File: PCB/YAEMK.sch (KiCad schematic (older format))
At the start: 222 parts, among them J1 DBG, P1 PC, P2 Link, P3 SSD1107, Q1 MMUN2133LT1G, Q2 DMMT5401, Q3 AO3401A, SW1 ALPS EC11, U1 24LC64, U2 SSP6206, U3 USBLC6-2SC6, U4 USBLC6-2SC6, U5 STM32F303CCTx

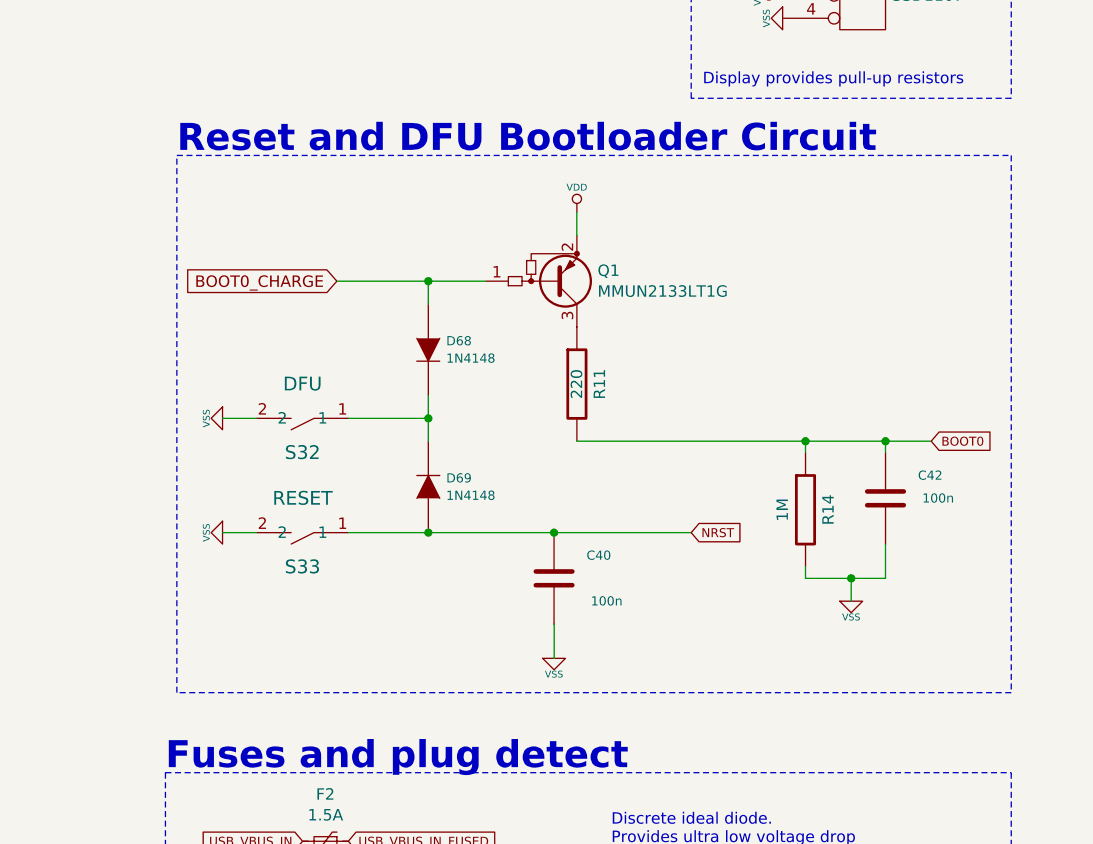
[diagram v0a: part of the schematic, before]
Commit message: Update Reset / DFU circut to single button version
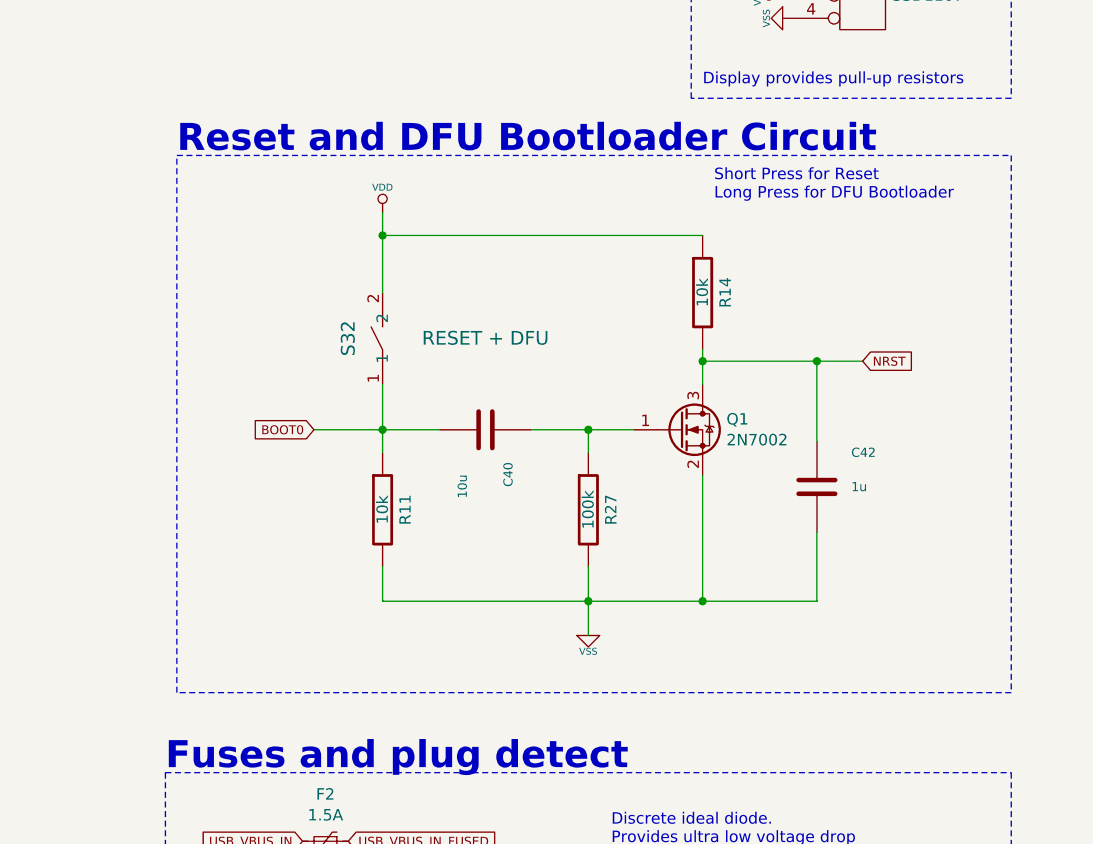
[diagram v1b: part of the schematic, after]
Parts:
- removed D68, D69: 1N4148, prettylib:D_SOD-523, symbol YAEMK:DIODE
- removed Q1: MMUN2133LT1G, prettylib:SOT-23, symbol Device:Q_PNP_BEC_BRT
- removed S33: RESET, prettylib:SMD_Tacticle_Switch_TS24CA_flipable, symbol YAEMK:SW
- added Q1: 2N7002, prettylib:SOT-23, symbol YAEMK:2N7002
- added R27: 100k, prettylib:SMD-0603, symbol YAEMK:R
- C40: value 100n -> 10u; LCSC Part C14663 -> C19702
- C42: value 100n -> 1u; LCSC Part C14663 -> C15849
- G1, G2, MH10, MH11, MH12: JLCPCB BOM (none) -> 0
- R11: value 220 -> 10k; LCSC Part C22962 -> C25804
- R14: value 1M -> 10k; LCSC Part C22935 -> C25804
- S32: value DFU -> RESET + DFU
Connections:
- net BOOT0: now also C40.1, R11.1, S32.1; no longer C42.2, R11.2, R14.1
- net NRST: now also C42.1, R14.2, Q1.3 (D); no longer C40.2
- net VDD: now also R14.1, S32.2
- net VSS: now also C42.2, R11.2, Q1.2 (S), R27.2; no longer C40.1, C42.1, R14.2, S32.2
- new net: C40.2, Q1.1 (G), R27.1
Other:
- note added: "Short Press for Reset\nLong Press for DFU Bootloader"
- moved on the sheet: C40, R11

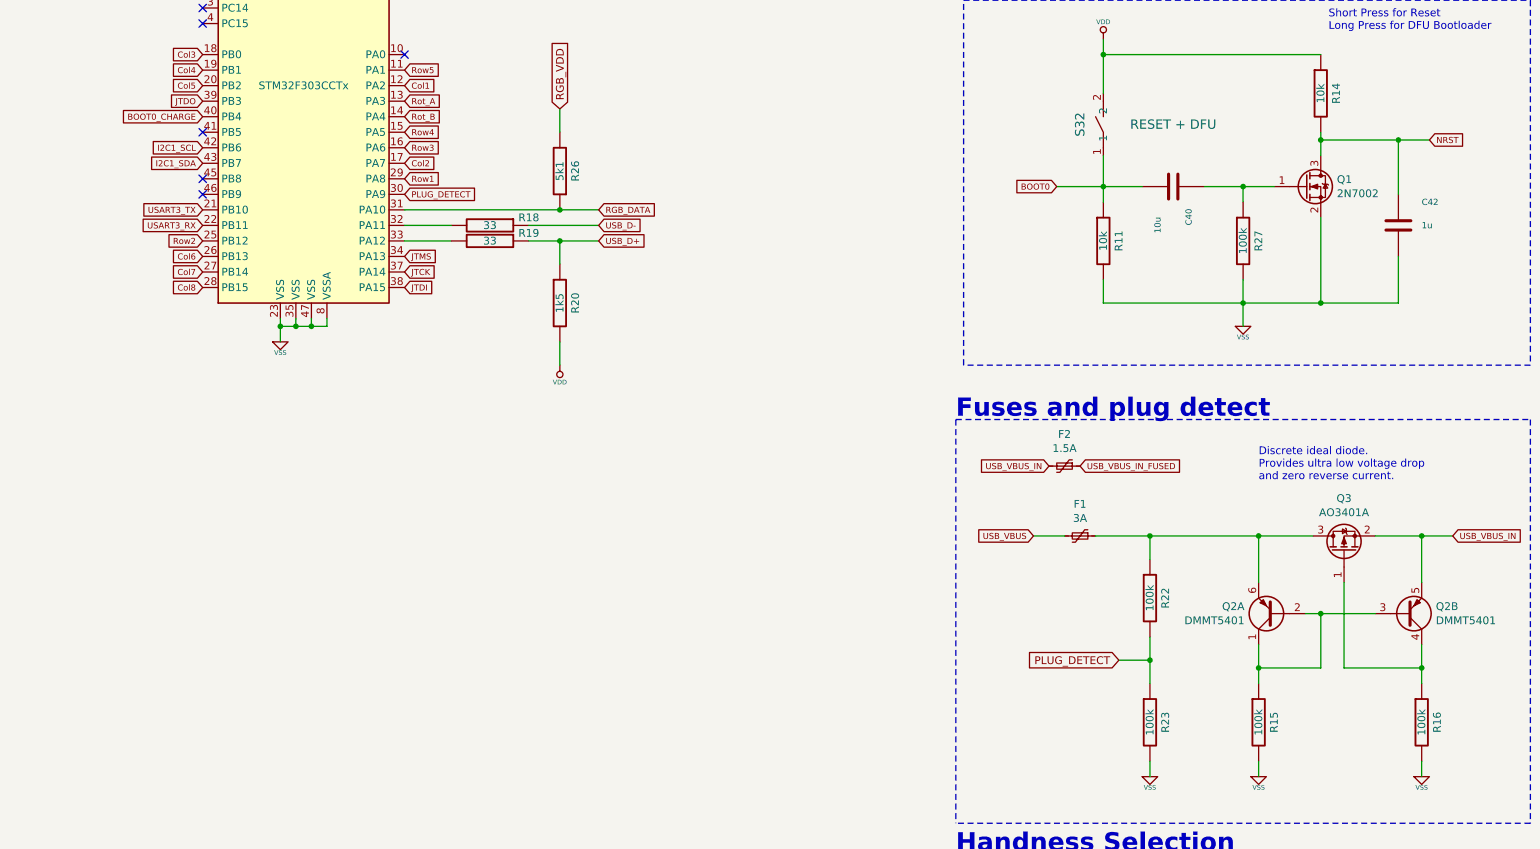
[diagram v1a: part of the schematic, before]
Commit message: Update Plugdetect Values
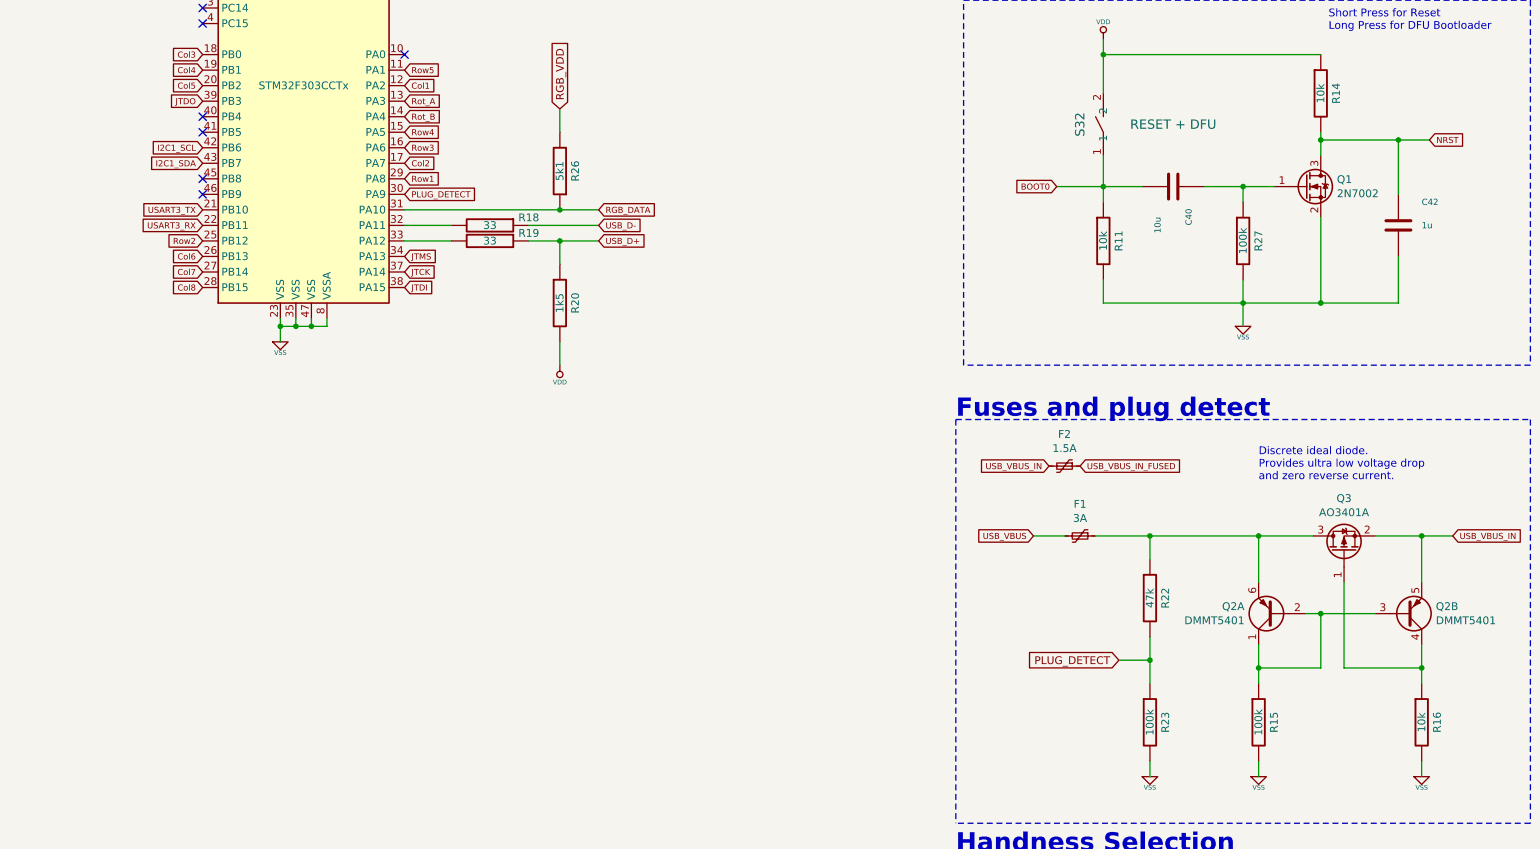
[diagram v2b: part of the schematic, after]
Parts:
- Q3: LCSC Part C15127 -> C142520
- R16: value 100k -> 10k
- R22: value 100k -> 47k
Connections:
- net BOOT0_CHARGE: no longer names the net of U5.40 (PB4)
- no-connect marks 14 -> 15
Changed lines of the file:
@@
 Text GLabel 15650 7300 2    39   Input ~ 0
 JTDI
-Text GLabel 14350 6200 0    39   Input ~ 0
-BOOT0_CHARGE
 Wire Notes Line
 	9400 800  9400 2900
@@
 P 22200 10100
 F 0 "R16" V 22300 10100 50  0000 C CNN
-F 1 "100k" V 22200 10100 50  0000 C CNN
+F 1 "10k" V 22200 10100 50  0000 C CNN
 F 2 "prettylib:SMD-0603" V 22100 10100 60  0001 C CNN
 F 3 "" H 22200 10100 60  0001 C CNN
@@
 F 2 "prettylib:SOT-23" H 21900 8925 50  0001 L CIN
 F 3 "http://www.aosmd.com/pdfs/datasheet/AO3401A.pdf" H 21700 9000 50  0001 L CNN
-F 4 " C15127 " H 21700 9000 50  0001 C CNN "LCSC Part"
+F 4 " C142520" H 21700 9000 50  0001 C CNN "LCSC Part"
 F 5 "1" H 21700 9000 50  0001 C CNN "JLCPCB BOM"
 	1    21700 9000
@@
 P 20450 9300
 F 0 "R22" V 20550 9300 50  0000 C CNN
-F 1 "100k" V 20450 9300 50  0000 C CNN
+F 1 "47k" V 20450 9300 50  0000 C CNN
 F 2 "prettylib:SMD-0603" V 20350 9300 60  0001 C CNN
 F 3 "" H 20450 9300 60  0001 C CNN
@@
 Text Notes 21600 5650 0    50   ~ 0
 Short Press for Reset\nLong Press for DFU Bootloader
+NoConn ~ 14350 6200
 $EndSCHEMATC

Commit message: Add opamp ideal diode
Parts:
- removed Q2: DMMT5401, prettylib:SOT-23-6, symbol Device:Q_DUAL_PNP_PNP_C1B1B2C2E2E1
- removed R15: 100k, prettylib:SMD-0603, symbol YAEMK:R
- removed R16: 10k, prettylib:SMD-0603, symbol YAEMK:R
- removed U3, U4: USBLC6-2SC6, prettylib:SOT-23-6, symbol YAEMK:USBLC6-2SC6
- added U3, U4: USBLC6-4SC6, prettylib:SOT-23-6, symbol Power_Protection:USBLC6-4SC6
- added U6: LMV321, prettylib:SOT-23-5, symbol Amplifier_Operational:LMV321
- C45: value 100n -> 10u; footprint prettylib:SMD-0603 -> prettylib:SMD-0805; LCSC Part C14663 -> C15850
- D1, D10, D11, D12, D13, D14, D15, D16, D17, D18, D19, D2, D20, D21, D22, D23, D24, D25, D26, D27, D28, D29, D3, D30, D31, D32, D33, D34, D4, D5, D6, D7, D8, D9: footprint prettylib:D_SOD-523 -> Diode_SMD:D_SOD-123
- R22: value 47k -> 100k
- R23: value 100k -> 200k; LCSC Part C25803 -> C25811
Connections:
- net ESD_LINK+ is gone; now on net LINK+: P2.A6 (D+), P2.B6 (D+)
- net ESD_LINK- is gone; now on net LINK-: P2.A7 (D-), P2.B7 (D-)
- net ESD_USB_D+ is gone; now on net USB_D+: P1.A6 (D+), P1.B6 (D+)
- net ESD_USB_D- is gone; now on net USB_D-: P1.A7 (D-), P1.B7 (D-)
- net LINK+: now also U4.3 (I/O2)
- net LINK-: now also U4.1 (I/O1)
- net RGB_VDD: now also U6.1 (+), U6.5 (V+)
- net USB_D+: now also U3.3 (I/O2)
- net USB_D-: now also U3.1 (I/O1)
- net USB_VBUS: now also U3.5 (VBUS)
- net USB_VBUS_IN_FUSED: now also U4.5 (VBUS)
- net VSS: now also U3.2 (GND), U4.2 (GND), U6.2 (V-)
- net at F1.1, Q3.3 (D), R22.1: now also U6.3 (-)
- net at Q3.1 (G): now also U6.4
- no-connect marks 15 -> 19
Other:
- moved on the sheet: Q3

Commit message: RC for real
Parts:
- C43, C44, C45: footprint prettylib:SMD-0805 -> prettylib:SMD-0603
- C46, C47: value 12p -> 20p; LCSC Part C38523 -> C1648
- D1, D10, D11, D12, D13, D14, D15, D16, D17, D18, D19, D2, D20, D21, D22, D23, D24, D25, D26, D27, D28, D29, D3, D30, D31, D32, D33, D34, D4, D5, D6, D7, D8, D9: footprint Diode_SMD:D_SOD-123 -> prettylib:D_SOD-123; LCSC Part C68948 -> C81598
- F1: LCSC Part C118413 -> C70085
- F2: LCSC Part C99563 -> C70081
- HSE1: LCSC Part C648984 -> C403948
- Q3: LCSC Part C142520 -> C15127
- R18, R19: LCSC Part C23138 -> C23140
- U1: value 24LC64 -> CAT24C512; LCSC Part C189763 -> C56096
- U3, U4: value USBLC6-4SC6 -> SRV0504; JLCPCB BOM (none) -> 1; LCSC Part (none) -> C384888

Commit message: Update ESD Diode, clean libs
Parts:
- C40: LCSC Part C19702 -> C19702
- C43, C44, C45: LCSC Part C15850 -> C19702
- U2: value SSP6206 -> XC6206P332MR
- U3, U4: symbol Power_Protection:USBLC6-4SC6 -> YAEMK:SRV0504
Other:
- note added: "MCU STM32F303 or STM32F103"
- note removed: "MCU F103, F303 or GDVF103"
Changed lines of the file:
@@
 F 2 "prettylib:SMD-0603" H 8288 4950 30  0001 C CNN
 F 3 "" H 8250 5100 60  0000 C CNN
-F 4 "C15850" H 8250 5100 50  0001 C CNN "LCSC Part"
+F 4 "C19702" H 8250 5100 50  0001 C CNN "LCSC Part"
 F 5 "1" H 8250 5100 50  0001 C CNN "JLCPCB BOM"
 	1    8250 5100
@@
 F 2 "prettylib:SMD-0603" H 9388 4950 30  0001 C CNN
 F 3 "" H 9350 5100 60  0000 C CNN
-F 4 "C15850" H 9350 5100 50  0001 C CNN "LCSC Part"
+F 4 "C19702" H 9350 5100 50  0001 C CNN "LCSC Part"
 F 5 "1" H 9350 5100 50  0001 C CNN "JLCPCB BOM"
 	1    9350 5100
@@
 USB_D+
 Wire Wire Line
-	14950 1050 14850 1050
+	14950 1050 14900 1050
 Wire Wire Line
 	15450 1050 15350 1050
@@
 F 2 "prettylib:SMD-0603" H 15188 900 30  0001 C CNN
 F 3 "" H 15150 1050 60  0000 C CNN
-F 4 "C15850" H 15150 1050 50  0001 C CNN "LCSC Part"
+F 4 "C19702" H 15150 1050 50  0001 C CNN "LCSC Part"
 F 5 "1" H 15150 1050 50  0001 C CNN "JLCPCB BOM"
 	1    15150 1050
@@
 Text GLabel 12850 1050 0    39   Input ~ 0
 USB_VBUS
-Text GLabel 14850 2200 3    39   Input ~ 0
+Text GLabel 14900 2200 3    39   Input ~ 0
 VSS
 Text Notes 12000 800  0    118  ~ 24
@@
 Text GLabel 14700 1050 0    39   Input ~ 0
 USB_VBUS_IN_FUSED
-Connection ~ 14850 1050
-Wire Wire Line
-	14850 1050 14700 1050
+Connection ~ 14900 1050
+Wire Wire Line
+	14900 1050 14700 1050
 Wire Wire Line
 	12950 1050 12850 1050
@@
 P 8800 4800
 F 0 "U2" H 8800 5042 50  0000 C CNN
-F 1 "SSP6206" H 8800 4951 50  0000 C CNN
+F 1 "XC6206P332MR" H 8800 4951 50  0000 C CNN
 F 2 "prettylib:SOT-23" H 8800 5000 50  0001 C CNN
 F 3 "" H 8900 4550 50  0001 C CNN
@@
 Wire Notes Line
 	12000 800  15800 800
-Text Notes 15550 14700 0    118  ~ 24
+Text Notes 15550 14750 0    118  ~ 24
 JLC PCBA Holes
-Text Notes 14200 14800 0    118  ~ 24
+Text Notes 14250 14850 0    118  ~ 24
 YAEMK Logos
 Wire Notes Line
@@
 Wire Wire Line
 	7550 11400 7550 11550
-Text Notes 13800 4000 0    118  ~ 24
-MCU F103, F303 or GDVF103
+Text Notes 13600 4000 0    118  ~ 24
+MCU STM32F303 or STM32F103
 Wire Notes Line
 	19200 12450 21500 12450
@@
 F 2 "prettylib:SMD-0603" H 20638 6500 30  0001 C CNN
 F 3 "" H 20600 6650 60  0000 C CNN
-F 4 " C19702" H 20600 6650 50  0001 C CNN "LCSC Part"
+F 4 "C19702" H 20600 6650 50  0001 C CNN "LCSC Part"
 F 5 "1" H 20600 6650 50  0001 C CNN "JLCPCB BOM"
 	1    20600 6650
@@
 $EndComp
 $Comp
-L Power_Protection:USBLC6-4SC6 U3
+L YAEMK:SRV0504 U3
 U 1 1 609C60B5
 P 12950 1700
 F 0 "U3" H 12950 2281 50  0000 C CNN
-F 1 "SRV0504" H 12950 2190 50  0000 C CNN
+F 1 "SRV0504" H 13200 1300 50  0000 C CNN
 F 2 "prettylib:SOT-23-6" H 12950 1200 50  0001 C CNN
 F 3 "" H 13150 2050 50  0001 C CNN
@@
 $EndComp
 Wire Wire Line
-	12950 1050 12950 1300
+	12950 1050 12950 1200
 Wire Wire Line
 	12950 2200 12950 2100
@@
 NoConn ~ 13350 1800
 $Comp
-L Power_Protection:USBLC6-4SC6 U4
+L YAEMK:SRV0504 U4
 U 1 1 60B72425
-P 14850 1700
-F 0 "U4" H 14850 2281 50  0000 C CNN
-F 1 "SRV0504" H 14850 2190 50  0000 C CNN
-F 2 "prettylib:SOT-23-6" H 14850 1200 50  0001 C CNN
-F 3 "" H 15050 2050 50  0001 C CNN
-F 4 "1" H 14850 1700 50  0001 C CNN "JLCPCB BOM"
-F 5 " C384888" H 14850 1700 50  0001 C CNN "LCSC Part"
-	1    14850 1700
-	1    0    0    -1
-$EndComp
-NoConn ~ 15250 1600
-NoConn ~ 15250 1800
-Wire Wire Line
-	14350 1600 14450 1600
-Wire Wire Line
-	14450 1800 14350 1800
-Wire Wire Line
-	14850 1050 14850 1300
-Wire Wire Line
-	14850 2200 14850 2100
+P 14900 1700
+F 0 "U4" H 14900 2281 50  0000 C CNN
+F 1 "SRV0504" H 15200 1300 50  0000 C CNN
+F 2 "prettylib:SOT-23-6" H 14900 1200 50  0001 C CNN
+F 3 "" H 15100 2050 50  0001 C CNN
+F 4 "1" H 14900 1700 50  0001 C CNN "JLCPCB BOM"
+F 5 " C384888" H 14900 1700 50  0001 C CNN "LCSC Part"
+	1    14900 1700
+	1    0    0    -1
+$EndComp
+NoConn ~ 15300 1600
+NoConn ~ 15300 1800
+Wire Wire Line
+	14350 1600 14500 1600
+Wire Wire Line
+	14500 1800 14350 1800
+Wire Wire Line
+	14900 1050 14900 1200
+Wire Wire Line
+	14900 2200 14900 2100
 $EndSCHEMATC

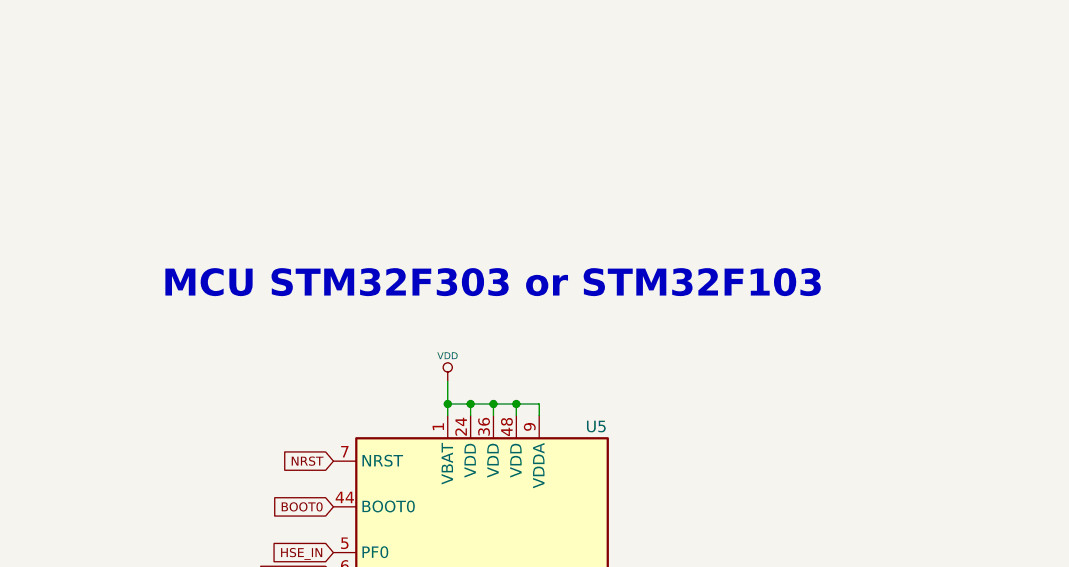
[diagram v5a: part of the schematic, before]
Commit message: Add GD32VF103 to schematic
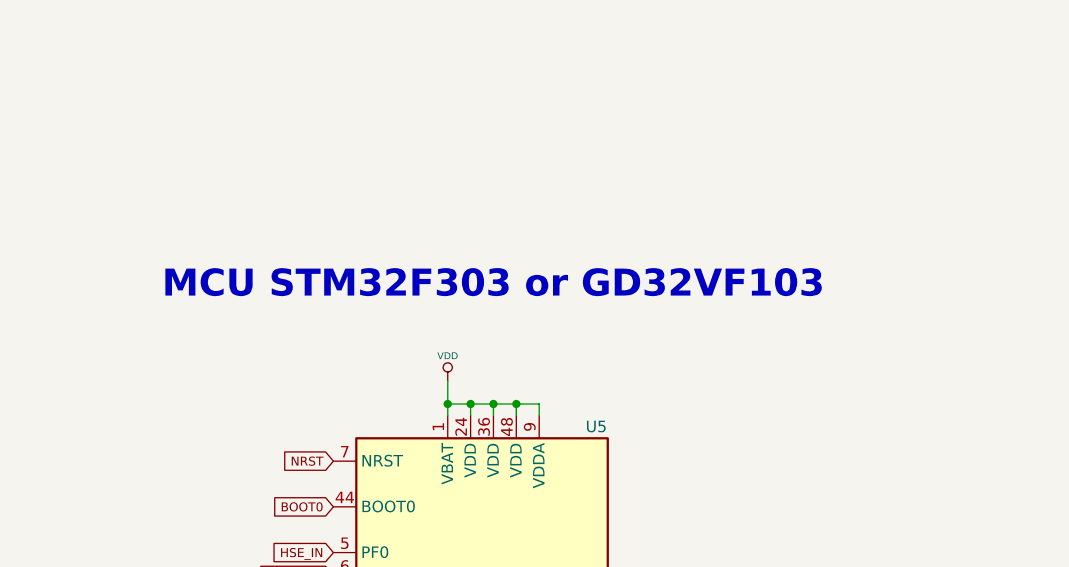
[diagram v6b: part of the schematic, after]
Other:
- note added: "MCU STM32F303 or GD32VF103"
- note removed: "MCU STM32F303 or STM32F103"
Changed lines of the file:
@@
 	7550 11400 7550 11550
 Text Notes 13600 4000 0    118  ~ 24
-MCU STM32F303 or STM32F103
+MCU STM32F303 or GD32VF103
 Wire Notes Line
 	19200 12450 21500 12450

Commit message: Replace discontinued led with blue one
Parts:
- D70: LCSC Part C268294 -> C72041
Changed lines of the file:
@@
 F 2 "prettylib:LED-0603_flipable" H 9700 4900 60  0001 C CNN
 F 3 "" H 9700 4800 60  0001 C CNN
-F 4 " C268294" H 9700 4800 50  0001 C CNN "LCSC Part"
+F 4 "C72041" H 9700 4800 50  0001 C CNN "LCSC Part"
 F 5 "1" H 9700 4800 50  0001 C CNN "JLCPCB BOM"
 	1    9700 4800

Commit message: Update pinheader not on backorder
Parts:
- J1: LCSC Part C376124 -> C56816
- U1: LCSC Part C56096 -> C56816
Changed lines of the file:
@@
 F 2 "prettylib:PinHeader_1x06_P2.54mm_Horizontal" H 8200 6550 50  0001 C CNN
 F 3 "~" H 8200 6550 50  0001 C CNN
-F 4 " C376124" H 8200 6550 50  0001 C CNN "LCSC Part"
+F 4 "C56816" H 8200 6550 50  0001 C CNN "LCSC Part"
 F 5 "1" H 8200 6550 50  0001 C CNN "JLCPCB BOM"
 	1    8200 6550
@@
 F 2 "prettylib:TSSOP-8_4.4x3mm_P0.65mm" H 21600 3450 50  0001 C CNN
 F 3 "" H 21600 3450 50  0001 C CNN
-F 4 "C56096" H 21600 3450 50  0001 C CNN "LCSC Part"
+F 4 "C56816" H 21600 3450 50  0001 C CNN "LCSC Part"
 F 5 "1" H 21600 3450 50  0001 C CNN "JLCPCB BOM"
 	1    21600 3450
